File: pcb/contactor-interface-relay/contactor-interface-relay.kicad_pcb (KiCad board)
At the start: 2 copper layers, 41.2 x 34.9 mm, 11 parts, among them J1 Conn_01x04_Socket, K1 G5LE-1

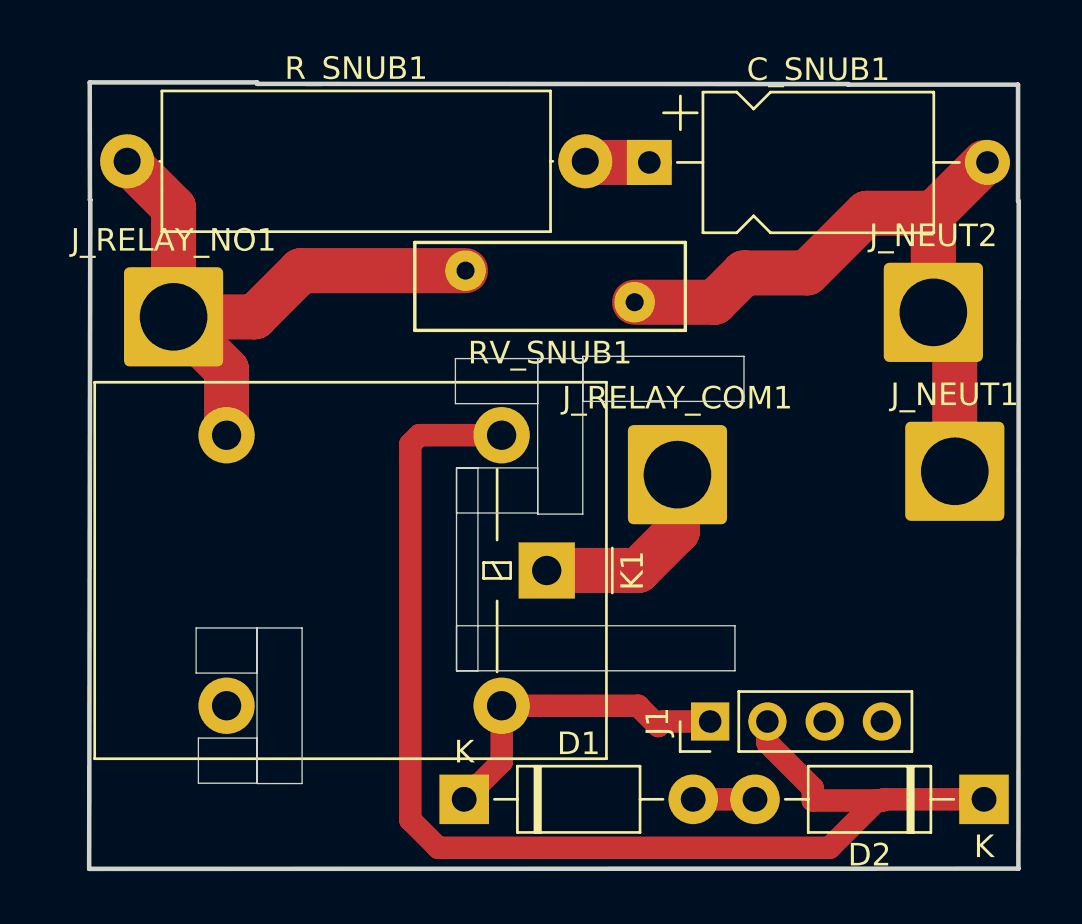
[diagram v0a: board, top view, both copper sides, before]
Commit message: Adding fuse for contactor coil
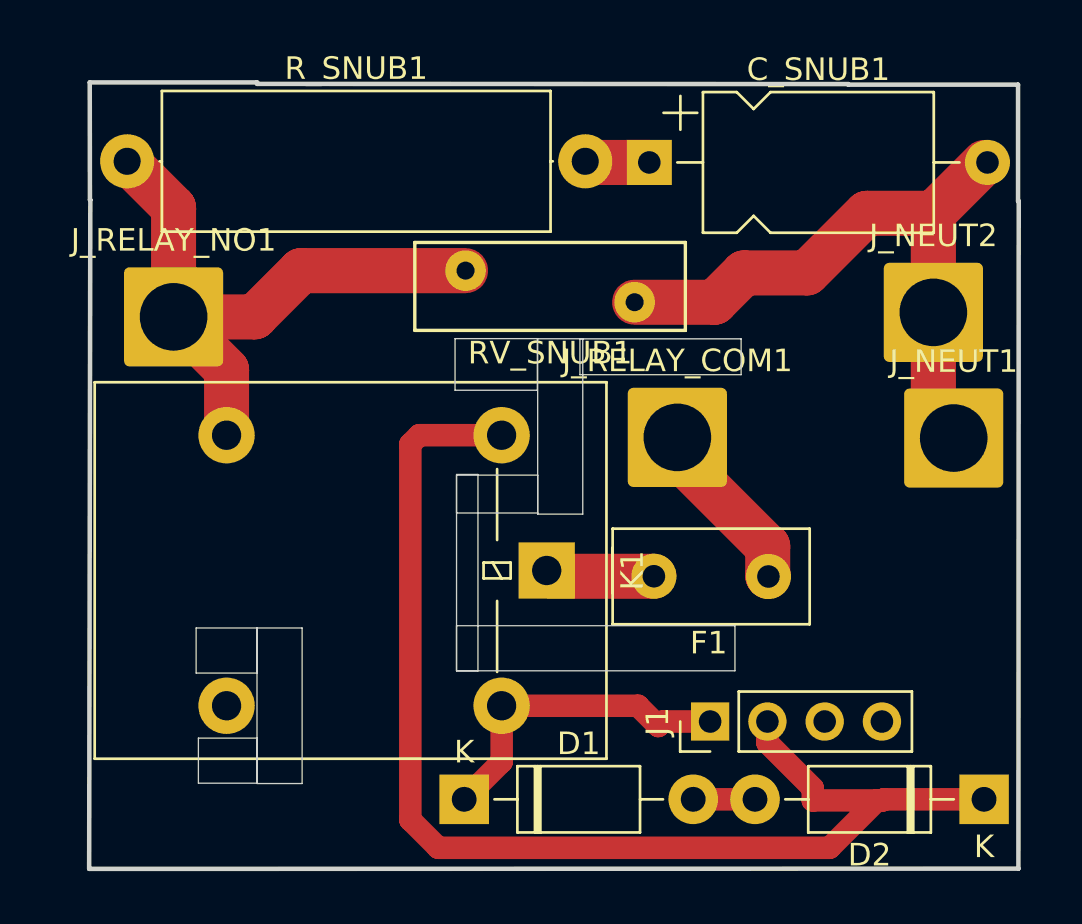
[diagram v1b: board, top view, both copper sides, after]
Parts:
- added F1: Fuse, Fuse:Fuse_Littelfuse_395Series, F.Cu at (30.2, 22.0)
- moved J_RELAY_COM1 1.65 mm to (26.2, 15.8)
- moved J_NEUT1 1.48 mm to (38.4, 15.9)
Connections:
- K1 pad 1: Net-(J_RELAY_COM1-Pin_1) -> Net-(F1-Pad2)
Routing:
- net Net-(F1-Pad2): track 0.00 -> 4.86 mm
- net Net-(J_RELAY_COM1-Pin_1): track 9.02 -> 7.93 mm
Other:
- outline, holes or cut-outs redrawn

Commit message: Extra 5v / ground connections
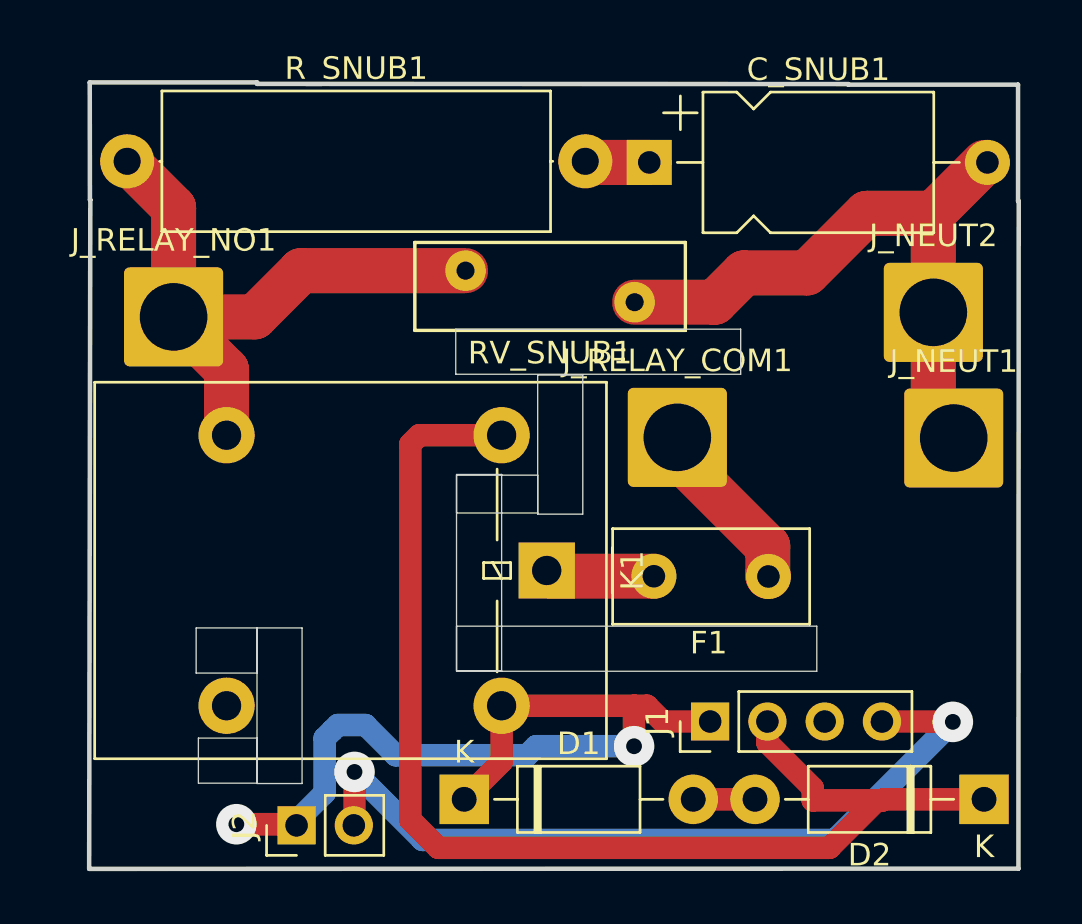
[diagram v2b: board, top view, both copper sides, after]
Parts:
- added J2: Conn_01x02_Socket, Connector_PinHeader_2.54mm:PinHeader_1x02_P2.54mm_Vertical, F.Cu at (9.27, 33.1)
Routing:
- net GND: track 0.00 -> 35.5 mm, vias 0 -> 2
- net +5V: track 14.5 -> 40.5 mm, vias 0 -> 2
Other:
- outline, holes or cut-outs redrawn

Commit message: Clearance fixes for contactor interface relay
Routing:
- net Net-(J_RELAY_COM1-Pin_1): track 7.93 -> 9.75 mm
- net GND: track 35.5 -> 34.3 mm
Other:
- outline, holes or cut-outs redrawn
